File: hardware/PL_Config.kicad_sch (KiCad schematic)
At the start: 37 parts, among them U2 xc7z020clg400

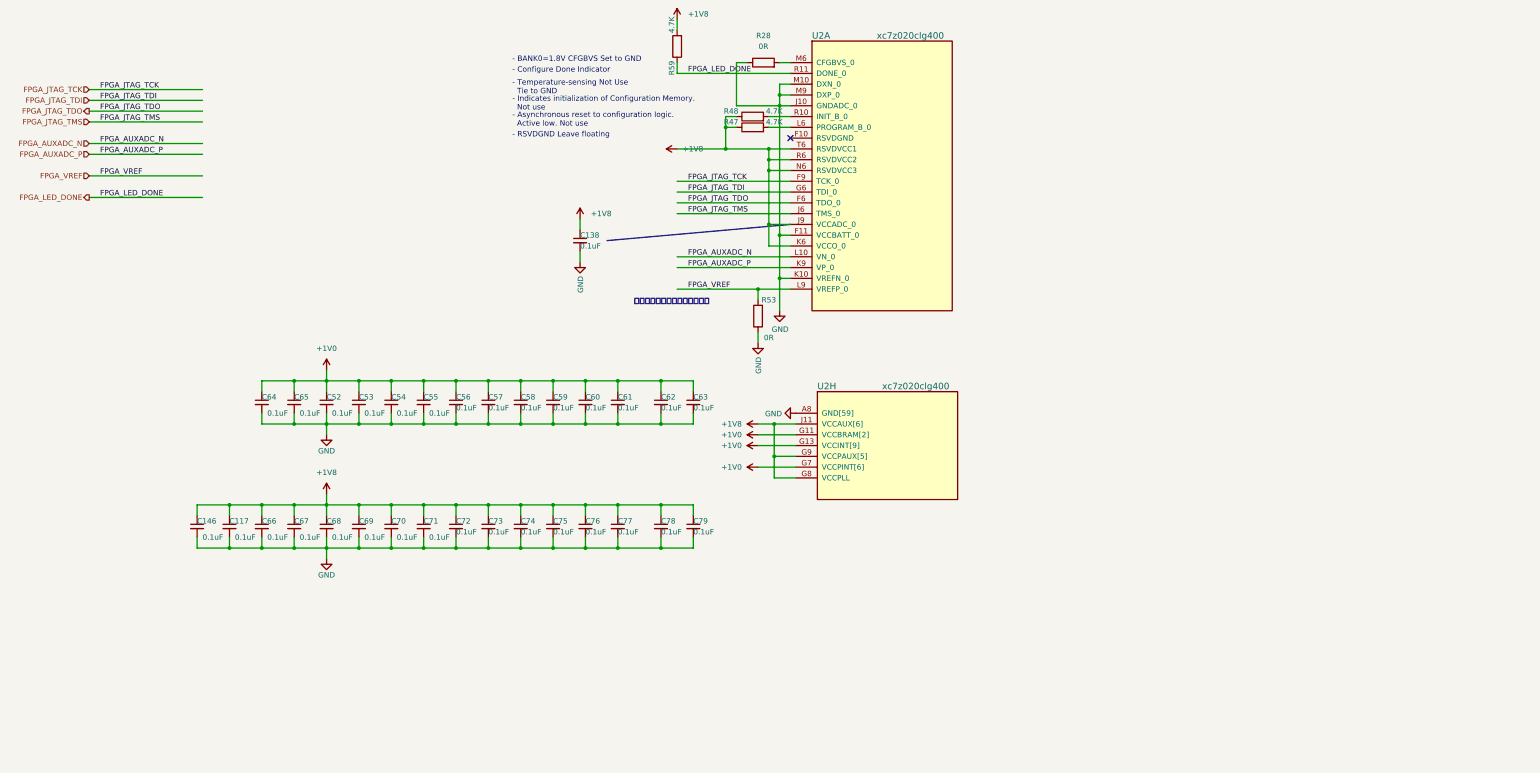
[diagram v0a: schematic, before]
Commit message: add sdio level shift ciruit
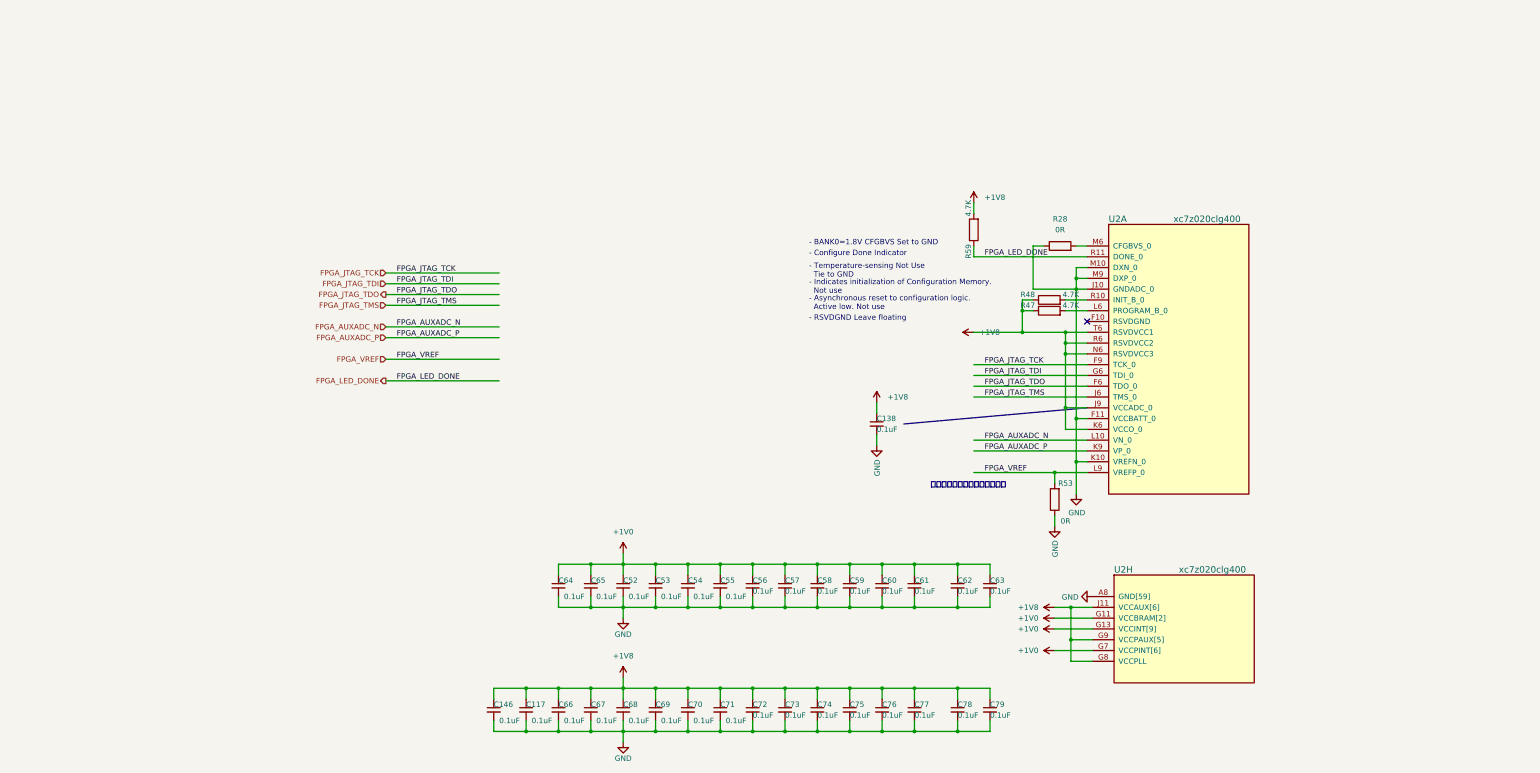
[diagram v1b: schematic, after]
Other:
- moved on the sheet: C117, C138, C146, C52, C53, C54, C55, C56, C57, C58, C59, C60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

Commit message: Modify wrong DCDC TPS62088 package Panelize PCB Add manufacture requirements files
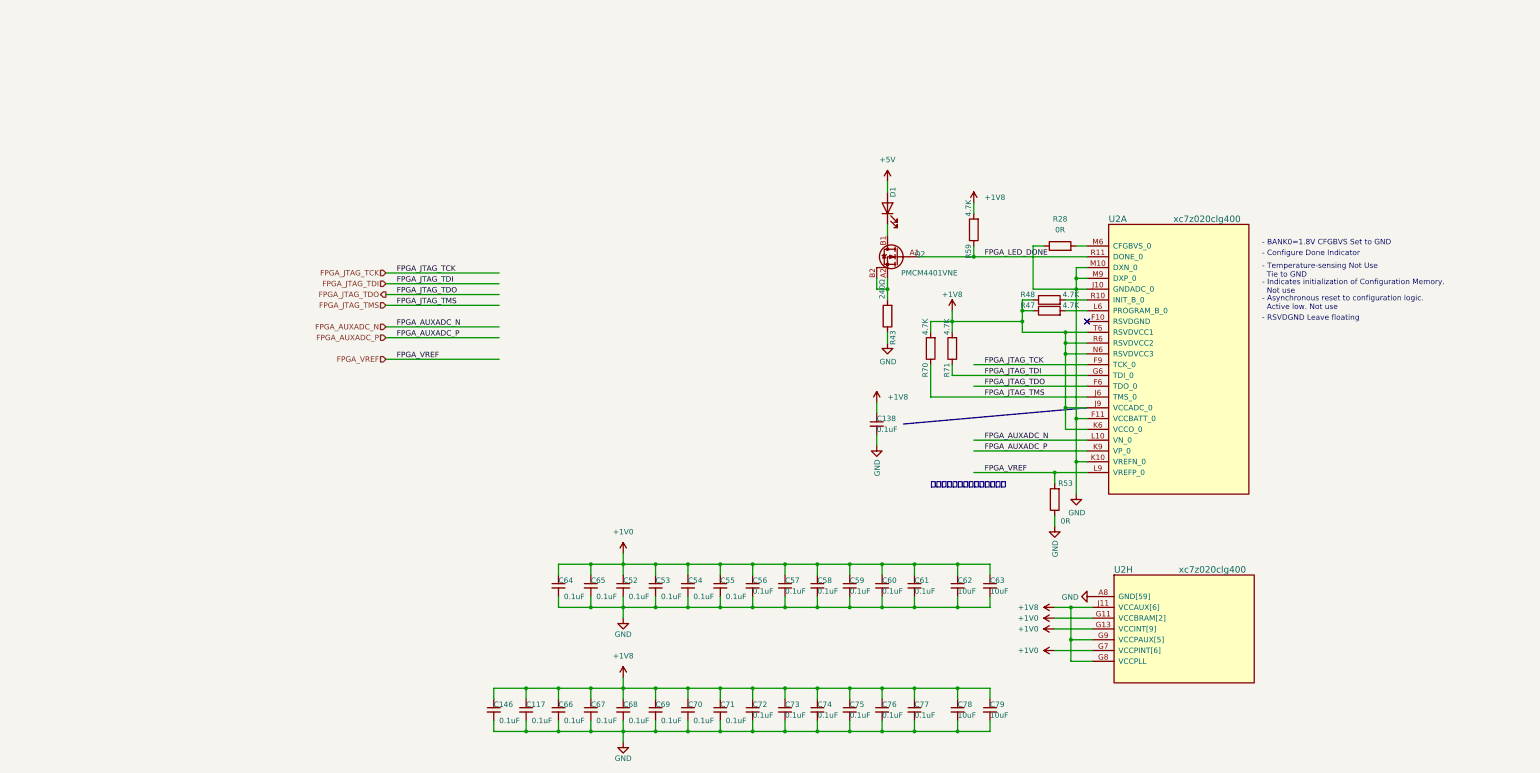
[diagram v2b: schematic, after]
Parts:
- added D1: LED, LED_SMD:LED_0201_0603Metric, symbol Device:LED
- added Q2: PMCM4401VNE, Package_CSP_Local:WLCSP-4-X1-WLB0909-4_0.89x0.89mm_P0.5mm, symbol Device:Q_NMOS_GDSD
- added R43: 240Ω, Resistor_SMD:R_0201_0603Metric, symbol Device:R
- added R70, R71: 4.7K, Resistor_SMD:R_0201_0603Metric, symbol Device:R
- C62, C63, C78, C79: value 0.1uF -> 10uF
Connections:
- net +1V8: now also R70.2, R71.2
- net FPGA_JTAG_TDI: now also R71.1
- net FPGA_JTAG_TMS: now also R70.1
- net FPGA_LED_DONE: now also Q2.A1 (G)
- net GND: now also R43.1
- new net: D1.1 (K), Q2.B1 (D)
- new net: Q2.A2 (S), Q2.B2 (D), R43.2
- new net +5V: D1.2 (A)
